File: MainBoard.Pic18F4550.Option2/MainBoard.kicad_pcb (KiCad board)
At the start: 2 copper layers, 90 parts, among them CON1 POWER_BUS, CON2 ICSP_CON, CON3 USB_CON, J1 RESET_CON, J2 SATA_PLUG _22P_SMT, J4 SATA_PLUG _22P_SMT, P1 DEBUG_HEADER_21P, P2 DEBUG_HEADER_21P, Q1 2N2222-SOT23, U1 PIC18F4550-I/P, U3 PCF85263A, Y1 Crystal, Y2 32.768KHZ

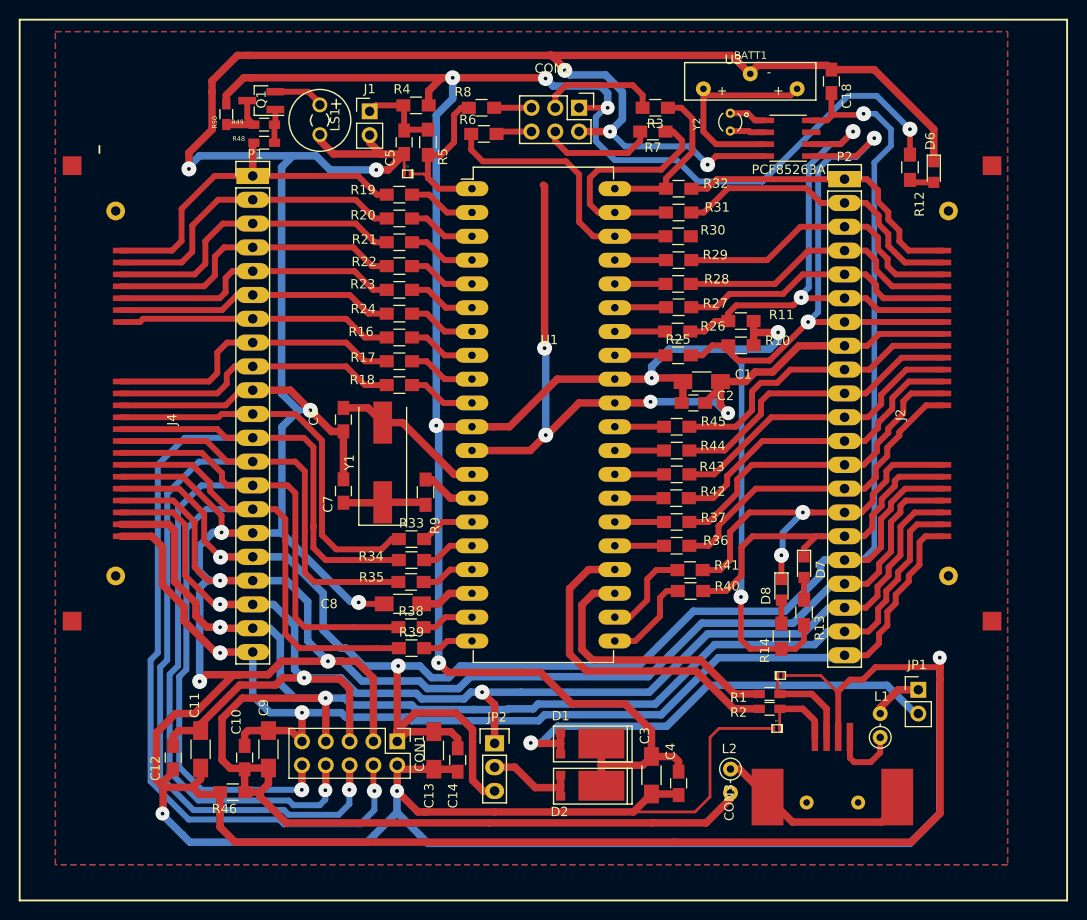
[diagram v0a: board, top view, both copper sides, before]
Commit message: Revision de PCbs + generacion de nuevos archivos Gerber
  - Se corrigen pads de pin headers
  - Se revisan
  - MainBoard option 2
  - PortExpander MC33996.Option3
  - GpibPortExpanderPCA6408A.Option3
  - Se generan Gerber + Vistas 3D
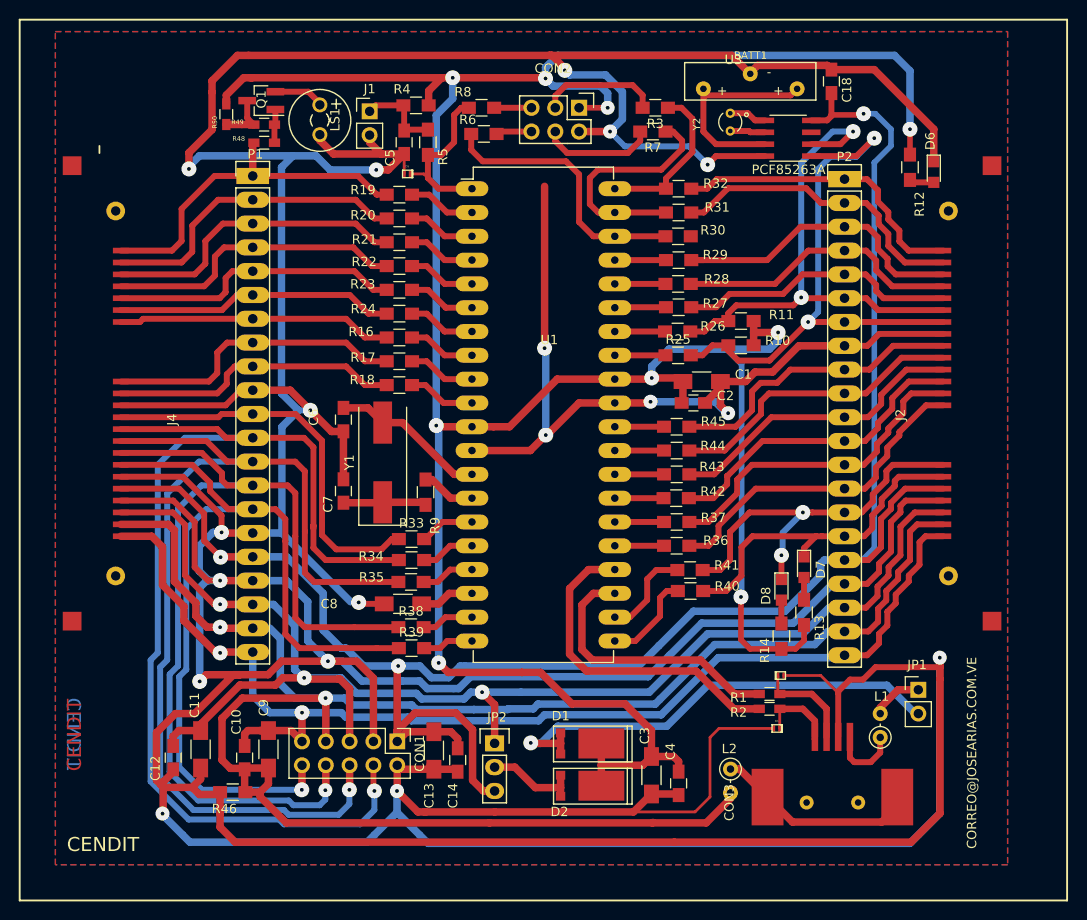
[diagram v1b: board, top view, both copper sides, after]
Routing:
- net VDD: track 299.6 -> 302.5 mm
- net /PB1: track 56.4 -> 57.3 mm
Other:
- board text added: "CENDIT"
- board text added: "CORREO@JOSEARIAS.COM.VE"
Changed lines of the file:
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@@
     (links 226)
     (no_connects 0)
-    (area 0 0 0 0)
+    (area 134.519999 39.972001 263.818572 144.880001)
     (thickness 1.6)
-    (drawings 7)
-    (tracks 1212)
+    (drawings 13)
+    (tracks 1204)
     (zones 0)
     (modules 90)
@@
     (tags "capacitor 0805")
     (attr smd)
-    (fp_text reference C18 (at -1.5748 1.6256 90) (layer F.SilkS)
+    (fp_text reference C18 (at -0.9144 1.651 90) (layer F.SilkS)
       (effects (font (size 1 1) (thickness 0.15)))
     )
-    (fp_text value 0.1uF (at 0.127 2.921 90) (layer F.Fab)
+    (fp_text value 0.1uF (at -0.2794 3.048 90) (layer F.Fab)
       (effects (font (size 1 1) (thickness 0.15)))
     )
@@
     )
   )
+  (gr_text CORREO@JOSEARIAS.COM.VE (at 236.22 128.905 90) (layer B.SilkS)
+    (effects (font (size 1 1) (thickness 0.25)) (justify mirror))
+  )
+  (gr_text CORREO@JOSEARIAS.COM.VE (at 236.22 129.032 90) (layer F.SilkS)
+    (effects (font (size 1 1) (thickness 0.25)))
+  )
+  (gr_text CENDIT (at 140.462 127 90) (layer B.Cu)
+    (effects (font (size 1.5 1.5) (thickness 0.3)) (justify mirror))
+  )
+  (gr_text CENDIT (at 140.462 127.127 90) (layer F.Cu)
+    (effects (font (size 1.5 1.5) (thickness 0.3)))
+  )
+  (gr_text CENDIT (at 143.51 138.811) (layer B.SilkS)
+    (effects (font (size 1.5 1.5) (thickness 0.25)) (justify mirror))
+  )
+  (gr_text CENDIT (at 143.51 138.811) (layer F.SilkS)
+    (effects (font (size 1.5 1.5) (thickness 0.25)))
+  )
   (dimension 88.9 (width 0.3) (layer F.SilkS)
     (gr_text 88,900mm (at 257.89 96.52 270) (layer F.SilkS)
@@
   (gr_line (start 134.62 50.8) (end 246.38 50.8) (angle 90) (layer F.SilkS) (width 0.2))
   (gr_line (start 143.129 65.024) (end 143.129 64.2747) (angle 90) (layer F.SilkS) (width 0.2))
+  (segment (start 192.024 54.61) (end 227.965 54.61) (width 0.8) (layer B.Cu) (net 1))
+  (segment (start 190.7286 55.9054) (end 192.024 54.61) (width 0.8) (layer B.Cu) (net 1))
+  (segment (start 229.616 65.198) (end 229.616 62.484) (width 0.6) (layer F.Cu) (net 1))
+  (via (at 229.616 62.484) (size 1.6) (drill 0.4) (layers F.Cu B.Cu) (net 1))
+  (segment (start 190.7286 55.9054) (end 190.7286 57.0738) (width 0.8) (layer B.Cu) (net 1))
+  (segment (start 229.616 56.261) (end 229.616 62.484) (width 0.8) (layer B.Cu) (net 1))
+  (segment (start 227.965 54.61) (end 229.616 56.261) (width 0.8) (layer B.Cu) (net 1))
+  (segment (start 191.5414 57.8866) (end 196.596 57.8866) (width 0.8) (layer B.Cu) (net 1))
+  (segment (start 190.7286 57.0738) (end 191.5414 57.8866) (width 0.8) (layer B.Cu) (net 1))
+  (segment (start 196.596 57.8866) (end 197.358 58.6486) (width 0.8) (layer B.Cu) (net 1))
+  (segment (start 197.358 58.6486) (end 197.358 60.198) (width 0.8) (layer B.Cu) (net 1))
   (segment (start 159.385 56.9976) (end 158.5214 56.9976) (width 0.8) (layer F.Cu) (net 1))
   (segment (start 156.6672 58.8518) (end 156.6672 59.7838) (width 0.8) (layer F.Cu) (net 1))
   (segment (start 158.5214 56.9976) (end 156.6672 58.8518) (width 0.8) (layer F.Cu) (net 1))
   (segment (start 197.358 60.198) (end 197.104 60.198) (width 0.8) (layer B.Cu) (net 1))
-  (segment (start 213.868 68.072) (end 215.5444 66.3956) (width 0.635) (layer B.Cu) (net 1))
-  (segment (start 207.01 68.072) (end 213.868 68.072) (width 0.635) (layer B.Cu) (net 1))
-  (segment (start 204.724 65.786) (end 207.01 68.072) (width 0.635) (layer B.Cu) (net 1))
-  (segment (start 198.12 65.786) (end 204.724 65.786) (width 0.635) (layer B.Cu) (net 1))
-  (segment (start 196.088 63.754) (end 198.12 65.786) (width 0.635) (layer B.Cu) (net 1))
-  (segment (start 196.088 61.214) (end 196.088 63.754) (width 0.635) (layer B.Cu) (net 1))
-  (segment (start 197.104 60.198) (end 196.088 61.214) (width 0.635) (layer B.Cu) (net 1))
   (segment (start 215.9 117.936) (end 217.4075 117.936) (width 0.6) (layer F.Cu) (net 1))
   (segment (start 218.313 117.0305) (end 218.313 115.396) (width 0.6) (layer F.Cu) (net 1))
@@
   (segment (start 211.6455 87.5665) (end 211.6455 112.3315) (width 0.6) (layer B.Cu) (net 1))
   (segment (start 210.0326 85.9536) (end 211.6455 87.5665) (width 0.6) (layer B.Cu) (net 1))
-  (segment (start 229.616 65.198) (end 229.616 62.484) (width 0.6) (layer F.Cu) (net 1))
-  (via (at 229.616 62.484) (size 1.6) (drill 0.4) (layers F.Cu B.Cu) (net 1))
-  (segment (start 226.06 58.928) (end 229.616 62.484) (width 0.635) (layer B.Cu) (net 1))
-  (segment (start 223.012 58.928) (end 226.06 58.928) (width 0.635) (layer B.Cu) (net 1))
-  (segment (start 215.5444 66.3956) (end 223.012 58.928) (width 0.635) (layer B.Cu) (net 1))
   (segment (start 180.8226 56.9976) (end 190.6524 56.9976) (width 0.8) (layer F.Cu) (net 1))
   (via (at 197.358 60.198) (size 1.5) (drill 0.4) (layers F.Cu B.Cu) (net 1))
   (segment (start 197.358 60.198) (end 194.31 60.198) (width 0.6) (layer F.Cu) (net 1))
-  (segment (start 197.358 58.6486) (end 197.358 60.198) (width 0.8) (layer B.Cu) (net 1))
-  (segment (start 196.596 57.8866) (end 197.358 58.6486) (width 0.8) (layer B.Cu) (net 1))
-  (segment (start 191.5414 57.8866) (end 196.596 57.8866) (width 0.8) (layer B.Cu) (net 1))
-  (segment (start 190.7286 57.0738) (end 191.5414 57.8866) (width 0.8) (layer B.Cu) (net 1))
   (via (at 190.7286 57.0738) (size 1.6) (drill 0.4) (layers F.Cu B.Cu) (net 1))
   (segment (start 190.6524 56.9976) (end 190.7286 57.0738) (width 0.8) (layer F.Cu) (net 1))
@@
   (segment (start 179.07 94.107) (end 178.943 94.107) (width 0.6) (layer B.Cu) (net 1))
   (segment (start 165.6334 92.4814) (end 167.894 94.742) (width 0.8) (layer F.Cu) (net 2))
-  (segment (start 167.894 94.742) (end 169.144 94.742) (width 0.8) (layer F.Cu) (net 2) (status 800000))
-  (segment (start 169.144 94.742) (end 169.164 94.722) (width 0.8) (layer F.Cu) (net 2) (status C00000))
-  (segment (start 169.164 94.722) (end 169.164 99.842) (width 0.8) (layer F.Cu) (net 2) (status C00000))
+  (segment (start 167.894 94.742) (end 169.144 94.742) (width 0.8) (layer F.Cu) (net 2))
+  (segment (start 169.144 94.742) (end 169.164 94.722) (width 0.8) (layer F.Cu) (net 2))
+  (segment (start 169.164 94.722) (end 169.164 99.842) (width 0.8) (layer F.Cu) (net 2))
   (segment (start 177.292 137.795) (end 178.181 138.684) (width 0.8) (layer B.Cu) (net 2))
   (segment (start 232.8164 119.888) (end 232.8164 118.9736) (width 0.8) (layer F.Cu) (net 2))
@@
   (segment (start 159.4866 105.5751) (end 162.5981 105.5751) (width 0.8) (layer B.Cu) (net 2))
   (segment (start 190.627 85.852) (end 190.627 68.58) (width 0.8) (layer F.Cu) (net 2))
-  (segment (start 190.627 68.58) (end 190.5 68.453) (width 0.8) (layer F.Cu) (net 2))
   (segment (start 190.754 95.123) (end 190.754 85.979) (width 0.8) (layer B.Cu) (net 2))
   (via (at 190.627 85.852) (size 1.6) (drill 0.4) (layers F.Cu B.Cu) (net 2))
@@
   (segment (start 178.181 62.531) (end 175.741 62.531) (width 0.635) (layer F.Cu) (net 3))
   (segment (start 175.741 62.531) (end 175.641 62.631) (width 0.635) (layer F.Cu) (net 3))
-  (segment (start 182.88 99.314) (end 180.975 99.314) (width 0.8) (layer F.Cu) (net 4) (status 400000))
+  (segment (start 182.88 99.314) (end 180.975 99.314) (width 0.8) (layer F.Cu) (net 4))
   (segment (start 180.975 99.314) (end 175.455 93.794) (width 0.8) (layer F.Cu) (net 4))
-  (segment (start 175.455 93.794) (end 173.355 93.794) (width 0.8) (layer F.Cu) (net 4) (status 800000))
-  (segment (start 169.164 92.222) (end 171.783 92.222) (width 0.8) (layer F.Cu) (net 4) (status 400000))
-  (segment (start 171.783 92.222) (end 173.355 93.794) (width 0.8) (layer F.Cu) (net 4) (status 800000))
+  (segment (start 175.455 93.794) (end 173.355 93.794) (width 0.8) (layer F.Cu) (net 4))
+  (segment (start 169.164 92.222) (end 171.783 92.222) (width 0.8) (layer F.Cu) (net 4))
+  (segment (start 171.783 92.222) (end 173.355 93.794) (width 0.8) (layer F.Cu) (net 4))
   (segment (start 173.276 93.873) (end 173.355 93.794) (width 0.5) (layer F.Cu) (net 4))
   (segment (start 169.164 102.342) (end 173.307 102.342) (width 0.8) (layer F.Cu) (net 5))
@@
   (segment (start 226.0092 79.0956) (end 226.0092 79.7433) (width 0.635) (layer F.Cu) (net 51))
   (segment (start 224.8916 77.978) (end 226.0092 79.0956) (width 0.635) (layer F.Cu) (net 51))
-  (segment (start 218.0082 80.4418) (end 218.0082 80.1878) (width 0.635) (layer B.Cu) (net 52))
+  (segment (start 218.0082 80.4418) (end 218.0082 66.0908) (width 0.635) (layer B.Cu) (net 52))
   (segment (start 222.1992 64.0842) (end 223.5454 62.738) (width 0.635) (layer F.Cu) (net 52))
   (via (at 223.5454 62.738) (size 1.6) (drill 0.4) (layers F.Cu B.Cu) (net 52))
   (segment (start 222.1992 64.0842) (end 219.0862 64.0842) (width 0.635) (layer F.Cu) (net 52))
+  (segment (start 221.361 62.738) (end 223.5454 62.738) (width 0.635) (layer B.Cu) (net 52))
+  (segment (start 218.0082 66.0908) (end 221.361 62.738) (width 0.635) (layer B.Cu) (net 52))
+  (segment (start 218.0082 80.4418) (end 218.0082 80.1878) (width 0.635) (layer B.Cu) (net 52))
   (via (at 218.0082 80.4418) (size 1.6) (drill 0.4) (layers F.Cu B.Cu) (net 52))
-  (segment (start 222.2246 64.0588) (end 223.5454 62.738) (width 0.635) (layer B.Cu) (net 52))
-  (segment (start 221.1832 64.0588) (end 222.2246 64.0588) (width 0.635) (layer B.Cu) (net 52))
-  (segment (start 218.821 66.421) (end 221.1832 64.0588) (width 0.635) (layer B.Cu) (net 52))
-  (segment (start 218.821 79.375) (end 218.821 66.421) (width 0.635) (layer B.Cu) (net 52))
-  (segment (start 218.0082 80.1878) (end 218.821 79.375) (width 0.635) (layer B.Cu) (net 52))
   (segment (start 210.232 82.9564) (end 210.232 82.122) (width 0.635) (layer F.Cu) (net 52))
   (segment (start 218.0844 80.518) (end 218.0082 80.4418) (width 0.635) (layer F.Cu) (net 52))

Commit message: Revision de PCBs + generacion nuevos gerber
  - Se hacen ligeras correcciones en los PCBs (5)
  - Se genera nuevamente archivo PCBs combinados
  - Se generan nuevos archivos gerber
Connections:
- R30 pad 2: /PB5 -> GNDD
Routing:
- net GNDD: track 859.5 -> 871.1 mm, vias 18 -> 19
- net /PB6: track 32.5 -> 31.2 mm
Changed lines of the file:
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@@
-(kicad_pcb (version 4) (host pcbnew 4.0.6-e0-6349~53~ubuntu14.04.1)
+(kicad_pcb (version 4) (host pcbnew 4.0.7-e2-6376~58~ubuntu16.04.1)
   (general
-    (links 226)
+    (links 227)
     (no_connects 0)
-    (area 134.519999 39.972001 263.818572 144.880001)
+    (area 0 0 0 0)
     (thickness 1.6)
     (drawings 13)
-    (tracks 1204)
+    (tracks 1207)
     (zones 0)
     (modules 90)
-    (nets 96)
+    (nets 95)
   )
   (page A4)
@@
   )
   (setup
-    (last_trace_width 0.8)
+    (last_trace_width 0.635)
     (user_trace_width 0.2)
     (user_trace_width 0.3)
@@
   (net 92 "Net-(D8-Pad2)")
   (net 93 //MCLR_INT)
-  (net 94 /PB5)
-  (net 95 "Net-(U3-Pad7)")
+  (net 94 "Net-(U3-Pad7)")
   (net_class Default "This is the default net class."
     (clearance 0.25)
@@
     (add_net /D+)
     (add_net /D-)
-    (add_net /PB5)
     (add_net /USB_VBUS)
     (add_net GNDPWR)
@@
       (net 52 /PB1))
     (pad 7 smd rect (at 2.475 -0.635) (size 1.97 0.6) (layers F.Cu F.Paste F.Mask)
-      (net 95 "Net-(U3-Pad7)"))
+      (net 94 "Net-(U3-Pad7)"))
     (pad 8 smd rect (at 2.475 -1.905) (size 1.97 0.6) (layers F.Cu F.Paste F.Mask)
       (net 10 /VDD_3V))
@@
       (net 25 /LVP))
     (pad 2 smd rect (at 1.35 0) (size 1.5 1.3) (layers F.Cu F.Paste F.Mask)
-      (net 94 /PB5))
+      (net 2 GNDD))
     (model Resistors_SMD.3dshapes/R_0805.wrl
       (at (xyz 0 0 0))
@@
   (segment (start 179.07 94.234) (end 179.07 94.107) (width 0.6) (layer F.Cu) (net 1))
   (segment (start 179.07 94.107) (end 178.943 94.107) (width 0.6) (layer B.Cu) (net 1))
+  (segment (start 208.026 66.2686) (end 208.026 66.294) (width 0.635) (layer B.Cu) (net 2))
+  (segment (start 209.55 73.914) (end 206.2264 73.914) (width 0.635) (layer F.Cu) (net 2) (status 800000))
+  (via (at 209.55 73.914) (size 1.6) (drill 0.4) (layers F.Cu B.Cu) (net 2))
+  (segment (start 209.55 67.818) (end 209.55 73.914) (width 0.635) (layer B.Cu) (net 2))
+  (segment (start 208.026 66.294) (end 209.55 67.818) (width 0.635) (layer B.Cu) (net 2))
   (segment (start 165.6334 92.4814) (end 167.894 94.742) (width 0.8) (layer F.Cu) (net 2))
   (segment (start 167.894 94.742) (end 169.144 94.742) (width 0.8) (layer F.Cu) (net 2))
@@
   (segment (start 226.1997 68.9991) (end 226.1997 70.2183) (width 0.635) (layer F.Cu) (net 47))
   (segment (start 225.0186 67.818) (end 226.1997 68.9991) (width 0.635) (layer F.Cu) (net 47))
-  (segment (start 206.2772 71.374) (end 207.6196 71.374) (width 0.635) (layer F.Cu) (net 48))
-  (segment (start 220.1164 70.358) (end 222.631 70.358) (width 0.635) (layer F.Cu) (net 48))
-  (segment (start 218.5416 68.7832) (end 220.1164 70.358) (width 0.635) (layer F.Cu) (net 48))
-  (segment (start 210.2104 68.7832) (end 218.5416 68.7832) (width 0.635) (layer F.Cu) (net 48))
-  (segment (start 207.6196 71.374) (end 210.2104 68.7832) (width 0.635) (layer F.Cu) (net 48))
+  (segment (start 206.2772 71.374) (end 208.28 71.374) (width 0.635) (layer F.Cu) (net 48) (status 400000))
+  (segment (start 209.296 70.358) (end 222.631 70.358) (width 0.635) (layer F.Cu) (net 48) (status 800000))
+  (segment (start 208.28 71.374) (end 209.296 70.358) (width 0.635) (layer F.Cu) (net 48))
   (segment (start 222.631 70.358) (end 224.9297 70.358) (width 0.635) (layer F.Cu) (net 48))
   (segment (start 229.0699 76.708) (end 233.172 76.708) (width 0.635) (layer F.Cu) (net 48))
